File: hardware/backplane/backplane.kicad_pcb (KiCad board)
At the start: 2 copper layers, 200 x 124 mm, 39 parts, among them J1 C96ABC, J2 C96ABC, J3 C96ABC, J4 C96ABC, J5 C96ABC, J6 C96ABC, J7 C96ABC, J8 C96ABC, J9 C96ABC, SW1 SW_SPDT, SW2 SW_Push, SW3 SW_SPDT, U1 74AHCT125, U2 NE556, U3 74HC00, U4 74HC00, X1 CXO_DIP8

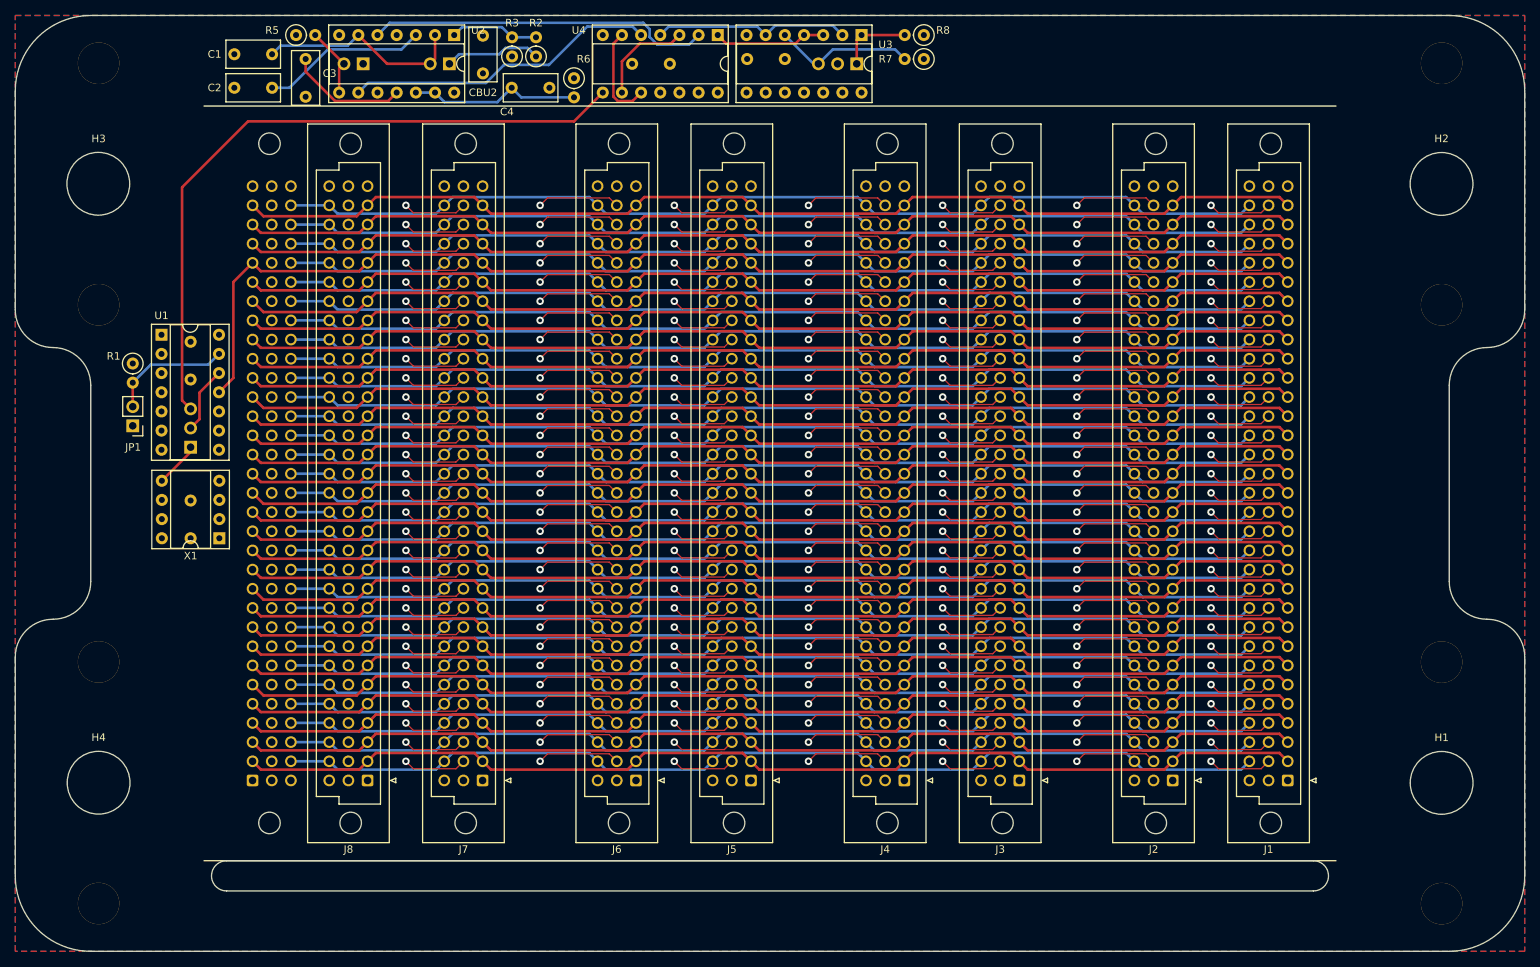
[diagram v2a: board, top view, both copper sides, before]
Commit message: backplane: shrink by 1mm in both dimensions and start rearranging components
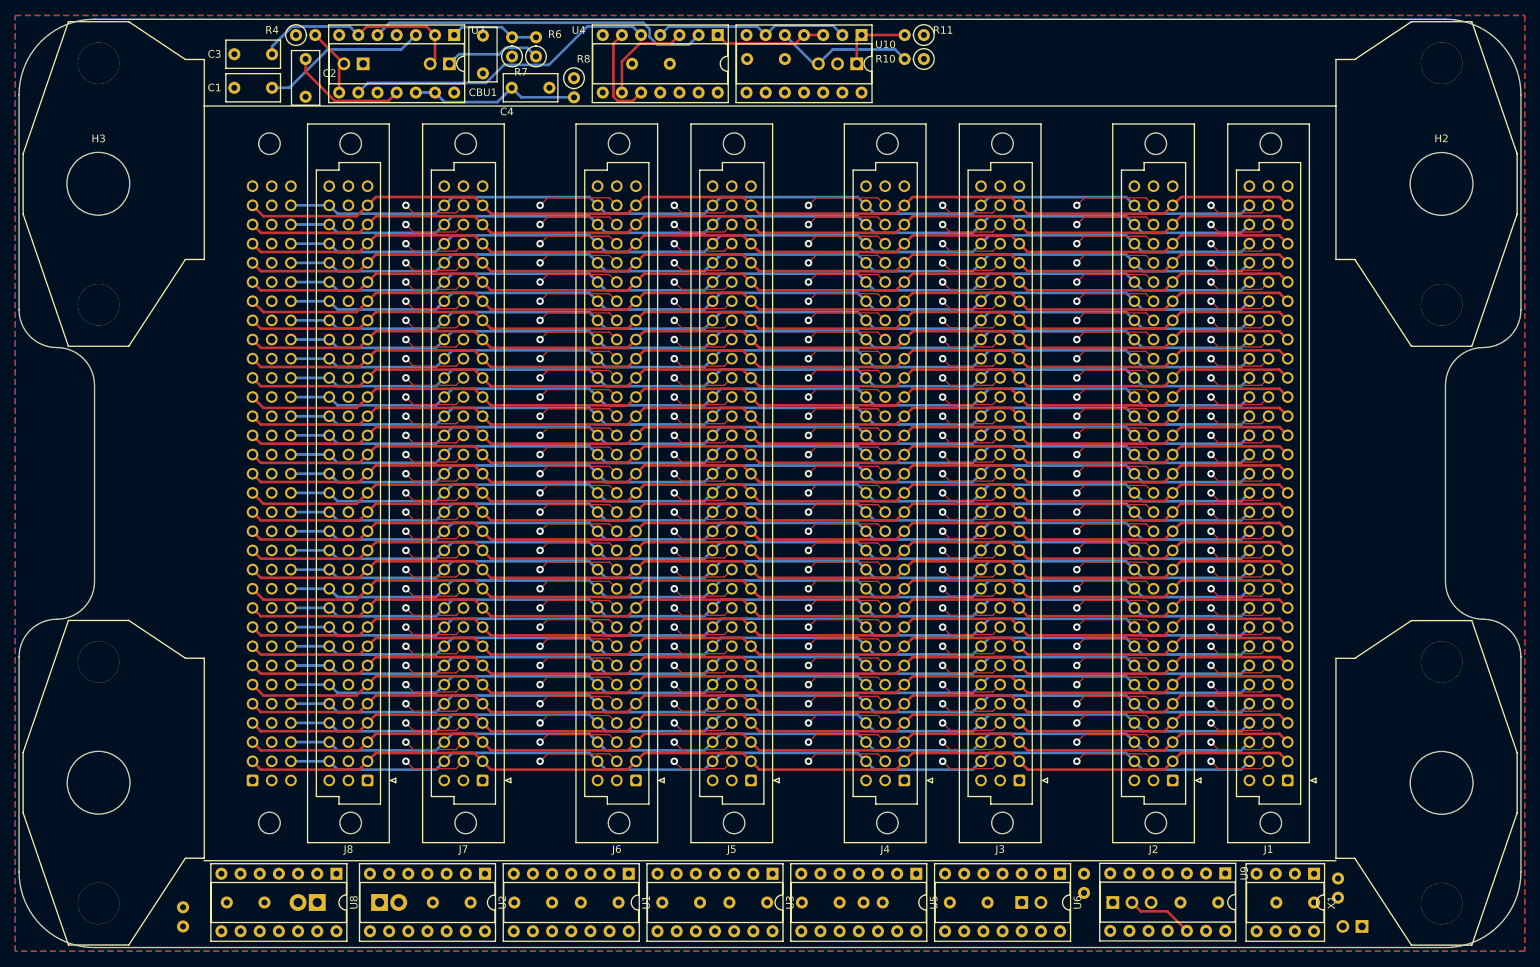
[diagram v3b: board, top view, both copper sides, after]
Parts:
- added CB1: 0.1μF, Capacitor_THT:C_Rect_L7.0mm_W3.5mm_P5.00mm, B.Cu at (104.4, 146.1)
- added CB2: 0.1μF, Capacitor_THT:C_Rect_L7.0mm_W3.5mm_P5.00mm, B.Cu at (77.1, 146.1)
- added CB3: 0.1μF, Capacitor_THT:C_Rect_L7.0mm_W3.5mm_P5.00mm, B.Cu at (172.9, 146.1)
- added CB4: 0.1μF, Capacitor_THT:C_Rect_L7.0mm_W3.5mm_P5.00mm, B.Cu at (115.2, 146.1)
- added CB5: 0.1μF, Capacitor_THT:C_Rect_L7.0mm_W3.5mm_P5.00mm, B.Cu at (153.3, 146.1)
- added CB6: 0.1μF, Capacitor_THT:C_Rect_L7.0mm_W3.5mm_P5.00mm, B.Cu at (138.7, 146.1)
- added CR1: 1μF, Capacitor_THT:C_Rect_L7.0mm_W3.5mm_P5.00mm, B.Cu at (119.0, 146.1)
- added CR2: 1μF, Capacitor_THT:C_Rect_L7.0mm_W3.5mm_P5.00mm, B.Cu at (129.8, 146.1)
- added D1: DIODE, Diode_THT:D_DO-15_P2.54mm_Vertical_AnodeUp, B.Cu at (92.3, 146.1)
- added D2: DIODE, Diode_THT:D_DO-15_P2.54mm_Vertical_AnodeUp, B.Cu at (84.1, 146.1)
- added JPC1: JP_RST, Connector_PinHeader_2.54mm:PinHeader_1x02_P2.54mm_Vertical, B.Cu at (177.4, 146.1)
- added R1: 4.7k, Resistor_THT:R_Axial_DIN0207_L6.3mm_D2.5mm_P2.54mm_Vertical, B.Cu at (66.3, 149.2)
- added R2: 1M, Resistor_THT:R_Axial_DIN0207_L6.3mm_D2.5mm_P2.54mm_Vertical, B.Cu at (185.7, 142.2)
- added R3: 100k, Resistor_THT:R_Axial_DIN0207_L6.3mm_D2.5mm_P2.54mm_Vertical, B.Cu at (159.0, 146.1)
- added U1: 74AHC14, Package_DIP:DIP-14_W7.62mm_Socket, F.Cu at (125.4, 142.2)
- added U2: 74AHC08, Package_DIP:DIP-14_W7.62mm_Socket, F.Cu at (106.3, 142.2)
- added U3: 74AHC08, Package_DIP:DIP-14_W7.62mm_Socket, F.Cu at (144.4, 142.2)
- added U5: 74AHC74, Package_DIP:DIP-14_W7.62mm_Socket, F.Cu at (163.5, 142.2)
- added U6: 74AHC74, Package_DIP:DIP-14_W7.62mm_Socket, F.Cu at (182.5, 142.2)
- added U8: 74AHC32, Package_DIP:DIP-14_W7.62mm_Socket, F.Cu at (86.6, 142.2)
- H1, H4, JP1: moved to B.Cu
- R9: renamed from R1; moved to B.Cu
- U10: renamed from U3; value 74HC00 -> U13
- moved JP1 175.9 mm to (222.5, 149.2), turned to 90 degrees
- moved R9 173.7 mm to (219.3, 142.9)
- moved U9 158.0 mm to (204.4, 142.2), turned to 270 degrees
- moved CBX1 156.5 mm to (216.2, 146.1), turned to 180 degrees
- moved CBU4 155.1 mm to (203.5, 146.1), turned to 180 degrees
- moved X1 151.7 mm to (216.2, 142.2), turned to 270 degrees
- moved SW2 136.3 mm to (189.5, 146.1), turned to 270 degrees
- turned H1 to 90 degrees
- turned H4 to 270 degrees
- renumbered C2 to C1, C3 to C2, C1 to C3, CBU2 to CBU1, CBU4 to CBU2, CBU1 to CBU4, R7 to R10, R8 to R11, R5 to R4, R4 to R5, R2 to R6, R3 to R7, R6 to R8, SW2 to SW1, SW1 to SW2, U2 to U7, U1 to U9
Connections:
- U9 pad 11: A28 -> Net-(U3-Pad1)
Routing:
- net 555_CLK: track 90.8 -> 0.00 mm
- net A28: track 163.4 -> 144.5 mm
- net ~CLK_ENABLE~: track 16.2 -> 0.00 mm
- net XO: track 6.02 -> 0.63 mm
- net Net-(C3-Pad1): track 27.7 -> 29.2 mm
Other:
- board size 200 x 124 mm -> 199 x 123 mm

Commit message: backplane: remove the base/bus clock switch
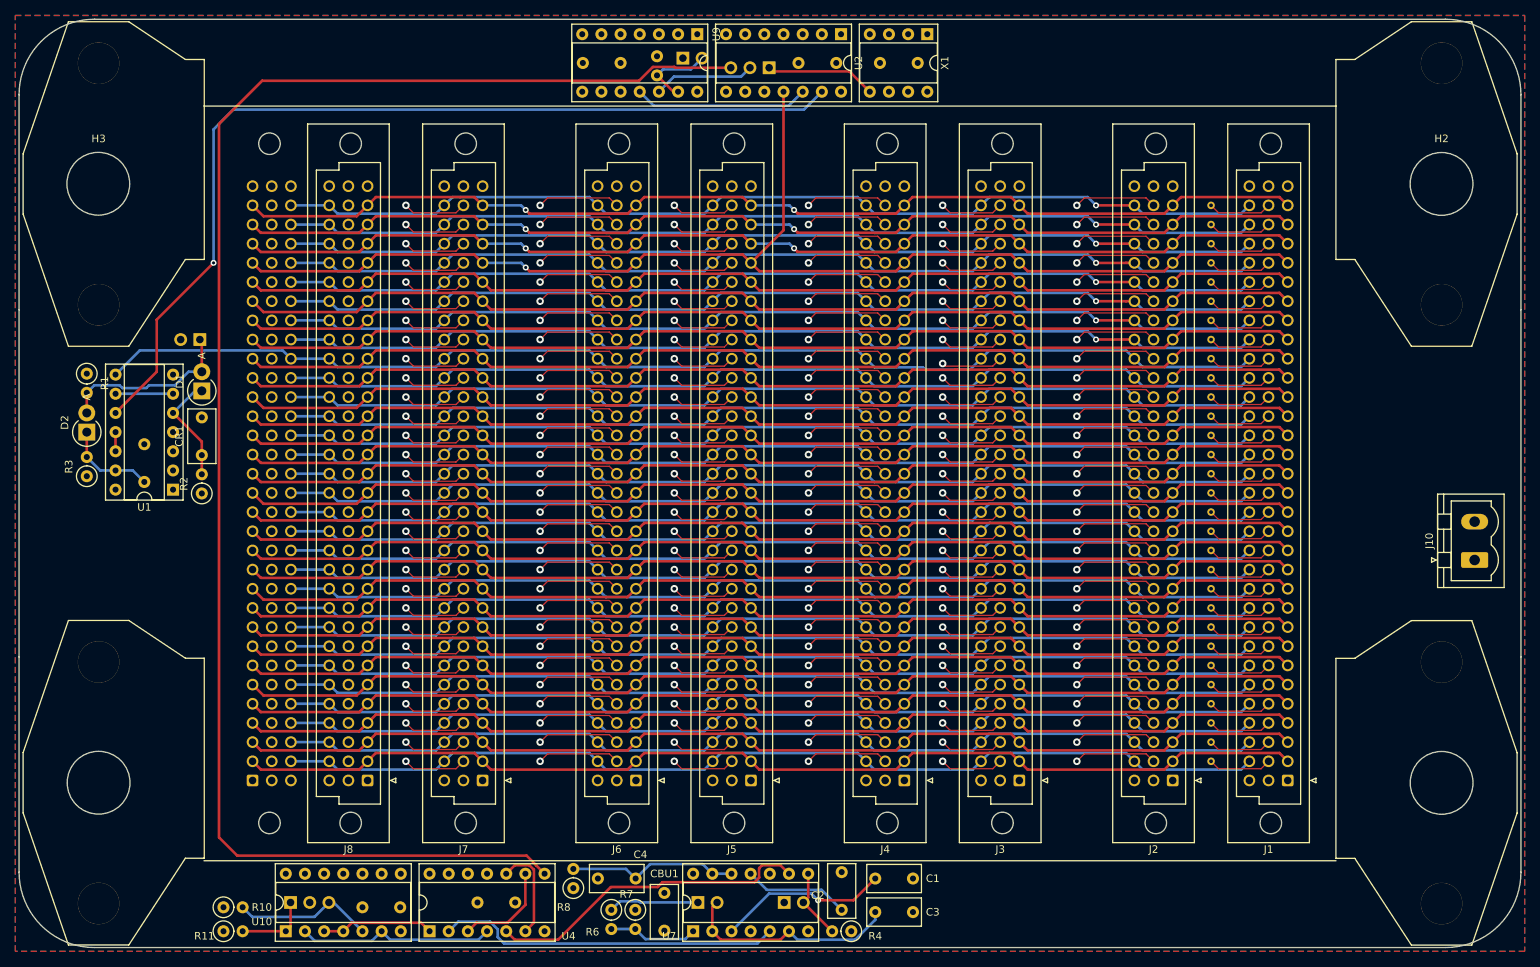
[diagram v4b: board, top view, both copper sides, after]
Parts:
- removed CB1, CB3, CB4, CB5, CB6: 0.1μF, Capacitor_THT:C_Rect_L7.0mm_W3.5mm_P5.00mm
- removed U3: 74AHC08, Package_DIP:DIP-14_W7.62mm_Socket
- removed U5, U6: 74AHC74, Package_DIP:DIP-14_W7.62mm_Socket
- removed U8: 74AHC32, Package_DIP:DIP-14_W7.62mm_Socket
- added J10: Conn_Coaxial_Power, Connector_Phoenix_MSTB:PhoenixContact_MSTBVA_2,5_2-G-5,08_1x02_P5.08mm_Vertical, F.Cu at (237.4, 100.7)
- added TP1: TestPoint, TestPoint:TestPoint_THTPad_D1.0mm_Drill0.5mm, B.Cu at (202.5, 127.3)
- added TP10: TestPoint, TestPoint:TestPoint_THTPad_D1.0mm_Drill0.5mm, B.Cu at (202.5, 104.5)
- added TP11: TestPoint, TestPoint:TestPoint_THTPad_D1.0mm_Drill0.5mm, B.Cu at (202.5, 101.9)
- added TP12: TestPoint, TestPoint:TestPoint_THTPad_D1.0mm_Drill0.5mm, B.Cu at (202.5, 99.4)
- added TP13: TestPoint, TestPoint:TestPoint_THTPad_D1.0mm_Drill0.5mm, B.Cu at (202.5, 96.9)
- added TP14: TestPoint, TestPoint:TestPoint_THTPad_D1.0mm_Drill0.5mm, B.Cu at (202.5, 94.3)
- added TP15: TestPoint, TestPoint:TestPoint_THTPad_D1.0mm_Drill0.5mm, B.Cu at (202.5, 91.8)
- added TP16: TestPoint, TestPoint:TestPoint_THTPad_D1.0mm_Drill0.5mm, B.Cu at (202.5, 89.2)
- added TP17: TestPoint, TestPoint:TestPoint_THTPad_D1.0mm_Drill0.5mm, B.Cu at (202.5, 86.7)
- added TP18: TestPoint, TestPoint:TestPoint_THTPad_D1.0mm_Drill0.5mm, B.Cu at (202.5, 84.2)
- added TP19: TestPoint, TestPoint:TestPoint_THTPad_D1.0mm_Drill0.5mm, B.Cu at (202.5, 81.6)
- added TP2: TestPoint, TestPoint:TestPoint_THTPad_D1.0mm_Drill0.5mm, B.Cu at (202.5, 124.8)
- added TP20: TestPoint, TestPoint:TestPoint_THTPad_D1.0mm_Drill0.5mm, B.Cu at (202.5, 79.1)
- added TP21: TestPoint, TestPoint:TestPoint_THTPad_D1.0mm_Drill0.5mm, B.Cu at (202.5, 76.5)
- added TP22: TestPoint, TestPoint:TestPoint_THTPad_D1.0mm_Drill0.5mm, B.Cu at (202.5, 74.0)
- added TP23: TestPoint, TestPoint:TestPoint_THTPad_D1.0mm_Drill0.5mm, B.Cu at (202.5, 71.5)
- added TP24: TestPoint, TestPoint:TestPoint_THTPad_D1.0mm_Drill0.5mm, B.Cu at (202.5, 68.9)
- added TP25: TestPoint, TestPoint:TestPoint_THTPad_D1.0mm_Drill0.5mm, B.Cu at (202.5, 66.4)
- added TP26: TestPoint, TestPoint:TestPoint_THTPad_D1.0mm_Drill0.5mm, B.Cu at (202.5, 63.8)
- added TP27: TestPoint, TestPoint:TestPoint_THTPad_D1.0mm_Drill0.5mm, B.Cu at (202.5, 61.3)
- added TP28: TestPoint, TestPoint:TestPoint_THTPad_D1.0mm_Drill0.5mm, B.Cu at (202.5, 58.8)
- added TP29: TestPoint, TestPoint:TestPoint_THTPad_D1.0mm_Drill0.5mm, B.Cu at (202.5, 56.2)
- added TP3: TestPoint, TestPoint:TestPoint_THTPad_D1.0mm_Drill0.5mm, B.Cu at (202.5, 122.3)
- added TP30: TestPoint, TestPoint:TestPoint_THTPad_D1.0mm_Drill0.5mm, B.Cu at (202.5, 53.7)
- added TP4: TestPoint, TestPoint:TestPoint_THTPad_D1.0mm_Drill0.5mm, B.Cu at (202.5, 119.7)
- added TP5: TestPoint, TestPoint:TestPoint_THTPad_D1.0mm_Drill0.5mm, B.Cu at (202.5, 117.2)
- added TP6: TestPoint, TestPoint:TestPoint_THTPad_D1.0mm_Drill0.5mm, B.Cu at (202.5, 114.6)
- added TP7: TestPoint, TestPoint:TestPoint_THTPad_D1.0mm_Drill0.5mm, B.Cu at (202.5, 112.1)
- added TP8: TestPoint, TestPoint:TestPoint_THTPad_D1.0mm_Drill0.5mm, B.Cu at (202.5, 109.6)
- added TP9: TestPoint, TestPoint:TestPoint_THTPad_D1.0mm_Drill0.5mm, B.Cu at (202.5, 107.0)
- CR1, D1, D2, R1, R2, R3: moved to F.Cu
- H4: footprint rails:SHF8-R -> rails:SHF8-L
- moved R11 150.7 mm to (71.7, 149.9), turned to 0 degrees
- moved JP1 146.1 mm to (132.5, 34.2), turned to 270 degrees
- moved R10 145.8 mm to (71.7, 146.7), turned to 0 degrees
- moved R9 141.5 mm to (129.1, 33.9)
- moved U10 141.1 mm to (79.9, 149.9), turned to 90 degrees
- moved R4 139.7 mm to (154.8, 149.9), turned to 180 degrees
- moved C3 138.9 mm to (158.0, 147.3), turned to 0 degrees
- moved SW3 134.1 mm to (80.6, 146.1), turned to 270 degrees
- moved C2 133.2 mm to (153.6, 147.0), turned to 90 degrees
- moved JPC1 132.0 mm to (68.5, 71.5), turned to 90 degrees
- moved C1 131.8 mm to (158.0, 142.9), turned to 0 degrees
- moved U9 131.4 mm to (134.4, 31.0)
- moved R2 127.3 mm to (68.8, 91.9), turned to 90 degrees
- moved CBU3 125.6 mm to (90.1, 146.7), turned to 0 degrees
- moved U4 124.7 mm to (99.0, 149.9), turned to 90 degrees
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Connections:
- net /RST-unused renamed Net-(U1-Pad6)
- net Net-(U1-Pad11) renamed CLK_RST
- D1 pad 2: C31 -> ~RST_HDR~
- D2 pad 2: C31 -> ~RST_HDR~
- JPC1 pad 1: C31 -> ~RST_HDR~
- R1 pad 2: C31 -> ~RST_HDR~
- U1 pad 1: A31 -> GND
- U1 pad 3: SYS_CLK -> GND
- U10 pad 10: Net-(U10-Pad10) -> GND
- U10 pad 12: Net-(U10-Pad12) -> GND
- U10 pad 13: Net-(U10-Pad13) -> GND
- U10 pad 9: Net-(U10-Pad9) -> GND
- U2 pad 1: BUS_ACTIVE -> GND
- U2 pad 10: Net-(U2-Pad10) -> GND
- U2 pad 11: Net-(U2-Pad11) -> A28
- U2 pad 13: SYS_CLK -> ~CLK_RST~
- U2 pad 2: Net-(U2-Pad2) -> GND
- U2 pad 4: A27 -> GND
- U2 pad 5: Net-(U2-Pad5) -> GND
- U2 pad 9: A31 -> GND
- U4 pad 12: Net-(U4-Pad12) -> GND
- U4 pad 13: Net-(U4-Pad13) -> GND
- U9 pad 1: Net-(U9-Pad1) -> VCC
- U9 pad 10: Net-(U9-Pad10) -> VCC
- U9 pad 11: Net-(U3-Pad1) -> Net-(U2-Pad12)
- U9 pad 2: Net-(U9-Pad2) -> GND
- U9 pad 4: Net-(U9-Pad4) -> VCC
- U9 pad 5: Net-(U9-Pad5) -> GND
- U9 pad 9: Net-(U9-Pad9) -> GND
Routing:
- net 555_CLK: track 0.00 -> 210.7 mm
- net ~CLK_RST~: track 0.00 -> 125.6 mm, vias 0 -> 1
- net C23: track 133.4 -> 158.7 mm
- net A28: track 144.5 -> 168.9 mm, vias 0 -> 1
- net ~RST_HDR~: track 0.00 -> 23.7 mm
- net Net-(U2-Pad12): track 0.00 -> 23.1 mm
- net Net-(CR1-Pad1): track 0.00 -> 14.7 mm
- net XO: track 0.63 -> 14.7 mm
- net Net-(CR2-Pad1): track 0.00 -> 12.3 mm
- net ~CLK_ENABLE~: track 0.00 -> 10.6 mm
- net Net-(U1-Pad6): track 0.00 -> 7.62 mm
- net Net-(SW2-Pad2): track 8.84 -> 13.4 mm
- net CLK_RST: track 0.00 -> 2.54 mm
- net Net-(C2-Pad1): track 15.8 -> 14.0 mm
- net 555_MONO: track 41.6 -> 43.2 mm
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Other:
- outline, holes or cut-outs redrawn
